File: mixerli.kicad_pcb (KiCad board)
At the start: 2 copper layers, 126 x 108 mm, 166 parts, among them J1 QingPu_WQP-PJ366ST, J10 Battery, J11 Battery, J2 QingPu_WQP-PJ366ST, J3 QingPu_WQP-PJ366ST, J4 QingPu_WQP-PJ366ST, J5 QingPu_WQP-PJ366ST, J6 QingPu_WQP-PJ366ST, J7 QingPu_WQP-PJ366ST, J8 UJC-HP-3-SMT-TR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

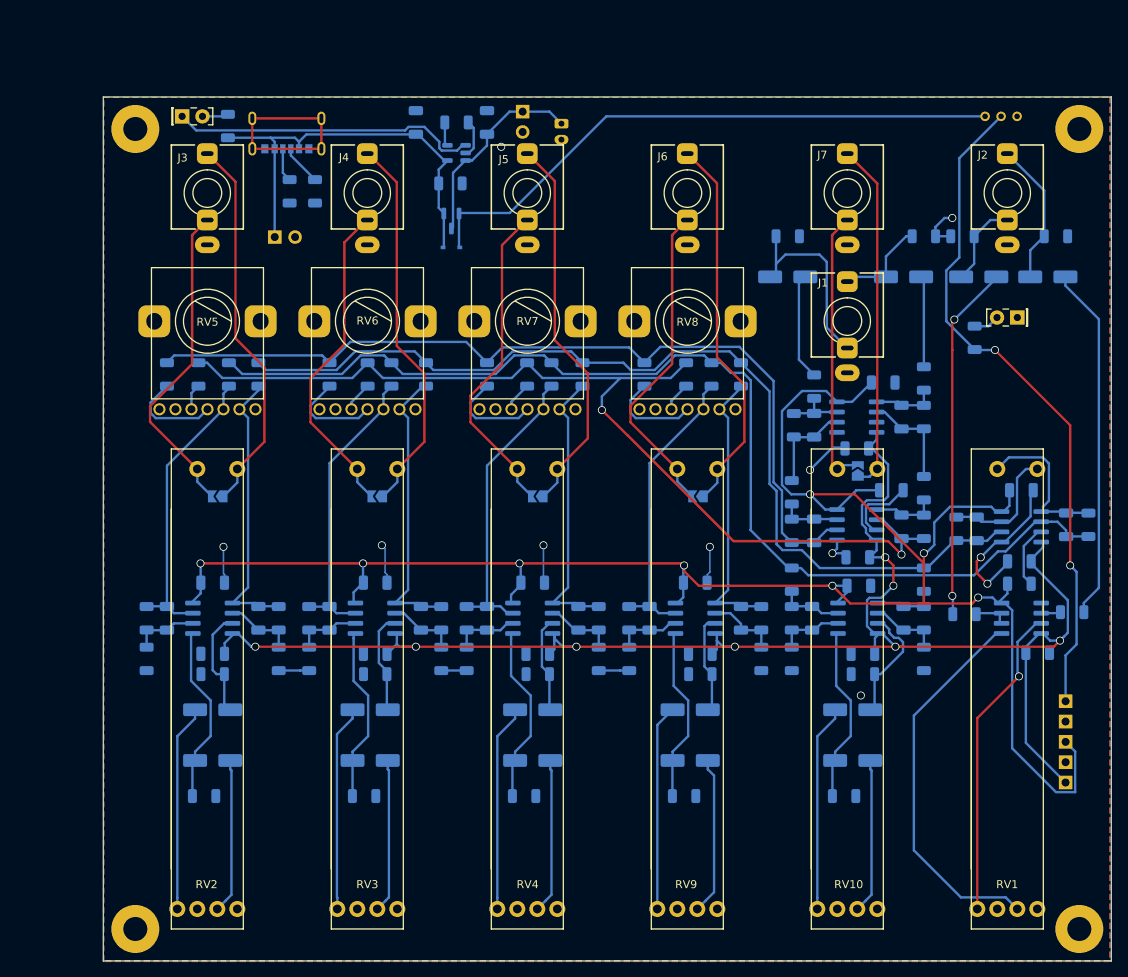
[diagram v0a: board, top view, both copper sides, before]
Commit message: metal sheet enclosure for 2.0 (charge led cutout missing!)
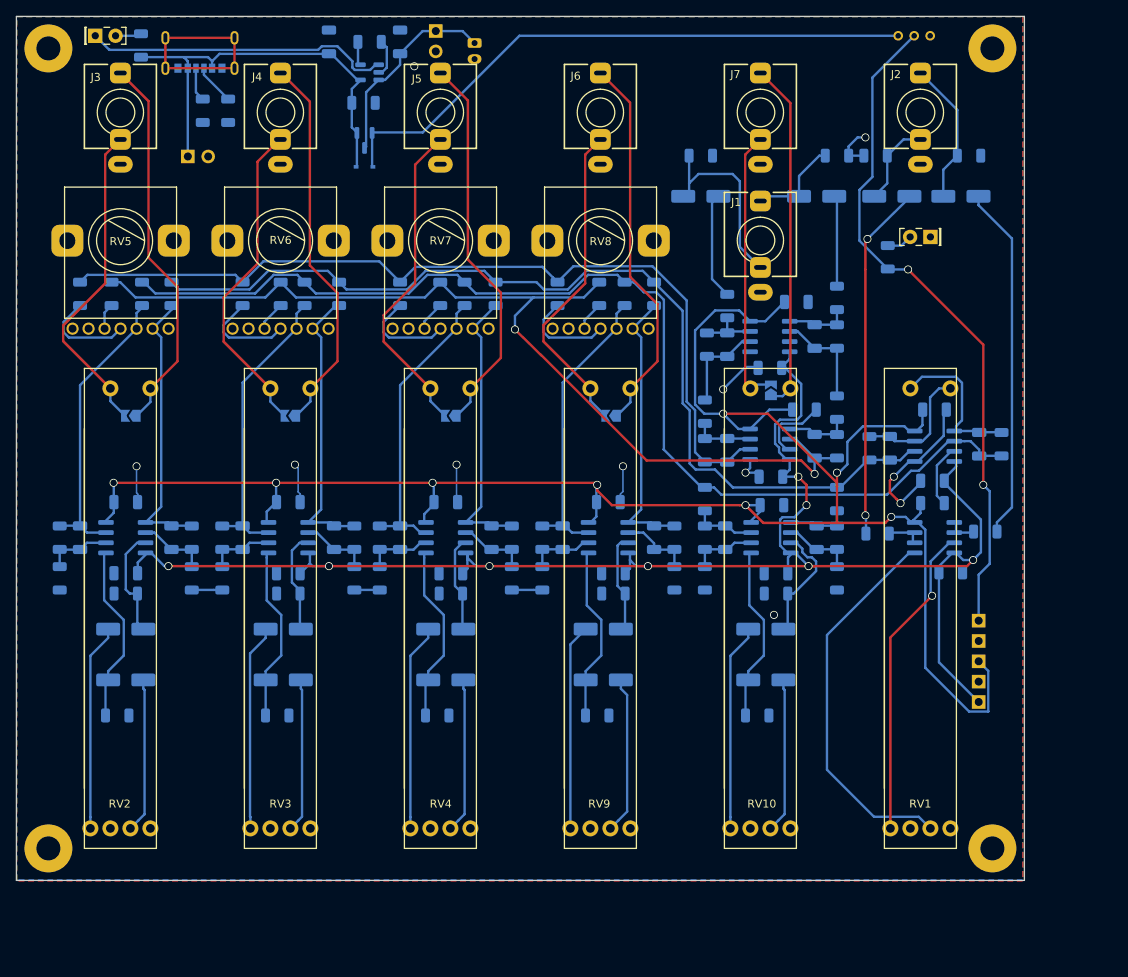
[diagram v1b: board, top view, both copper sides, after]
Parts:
- moved C1 14.8 mm to (180.3, 79.2)
- moved C11 14.8 mm to (195.0, 83.5)
- moved C12 14.8 mm to (195.3, 74.7)
- moved C14 14.8 mm to (195.0, 86.3)
- moved C3 14.8 mm to (174.8, 83.0)
- moved C33 14.8 mm to (134.8, 95.1)
- moved C39 14.8 mm to (155.1, 95.1)
- moved C4 14.8 mm to (179.0, 74.7)
- moved C40 14.8 mm to (154.5, 86.2)
- moved C41 14.8 mm to (174.2, 102.1)
- moved C42 14.8 mm to (174.2, 108.4)
- moved C46 14.8 mm to (175.0, 86.6)
- moved C50 14.8 mm to (128.5, 28.7)
- moved C8 14.8 mm to (189.7, 79.5)
- moved J10 14.8 mm to (137.8, 28.8)
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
